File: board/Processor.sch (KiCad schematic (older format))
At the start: 12 parts, among them U1 TM4C123GH6PM

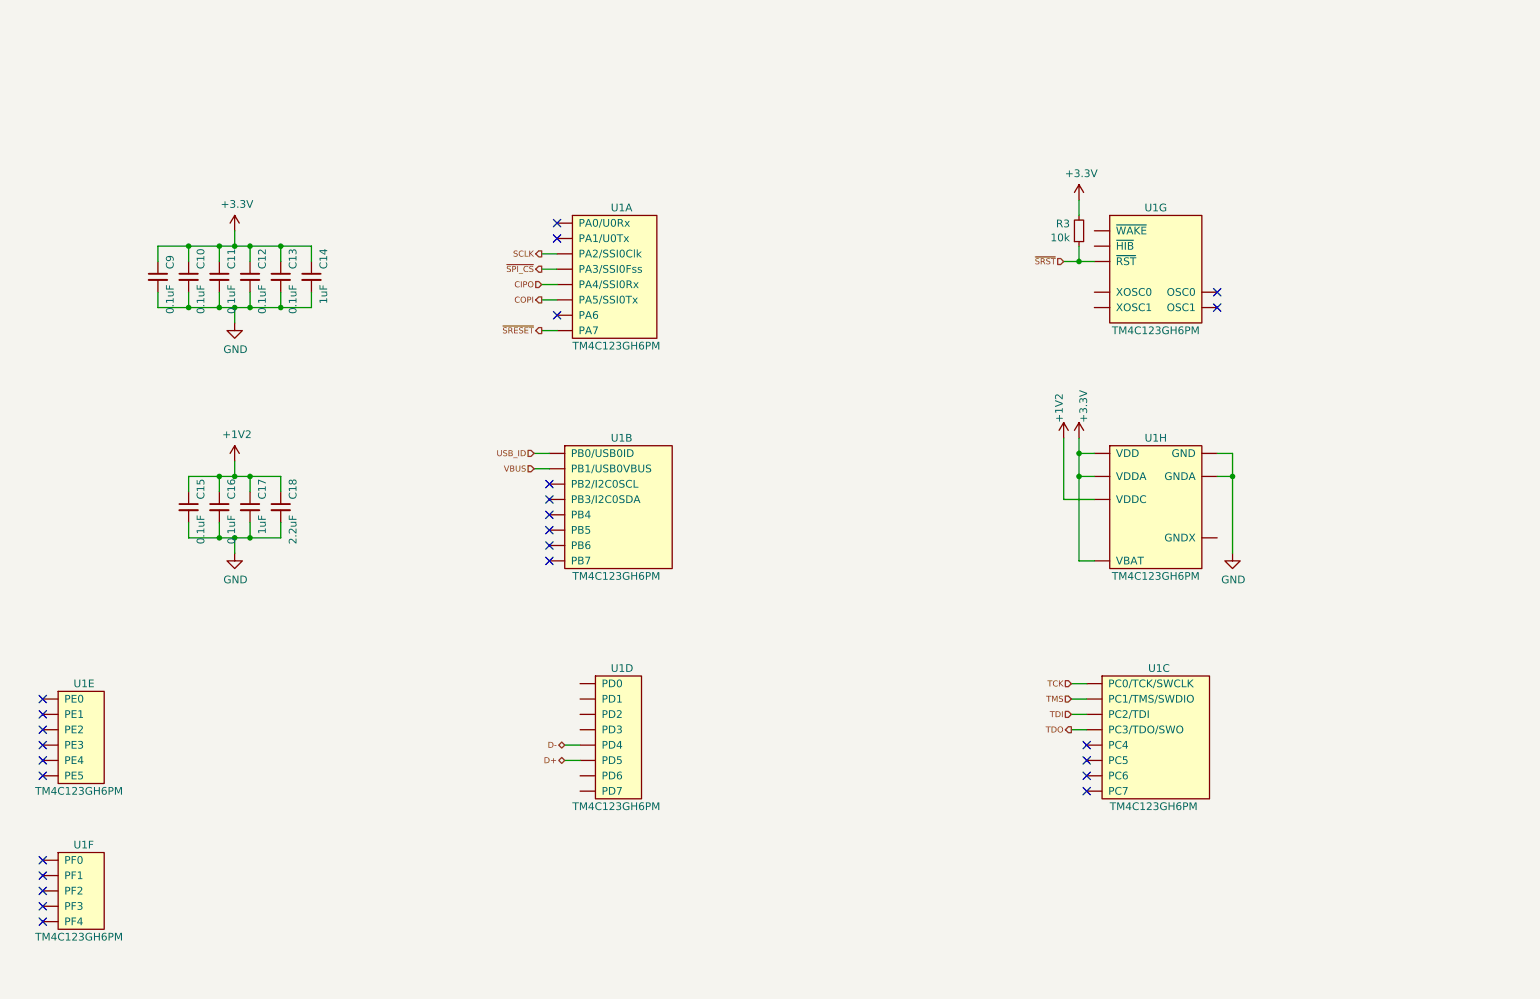
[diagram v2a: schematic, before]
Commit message: Added the two Flash devices and the user buttons to the schematic
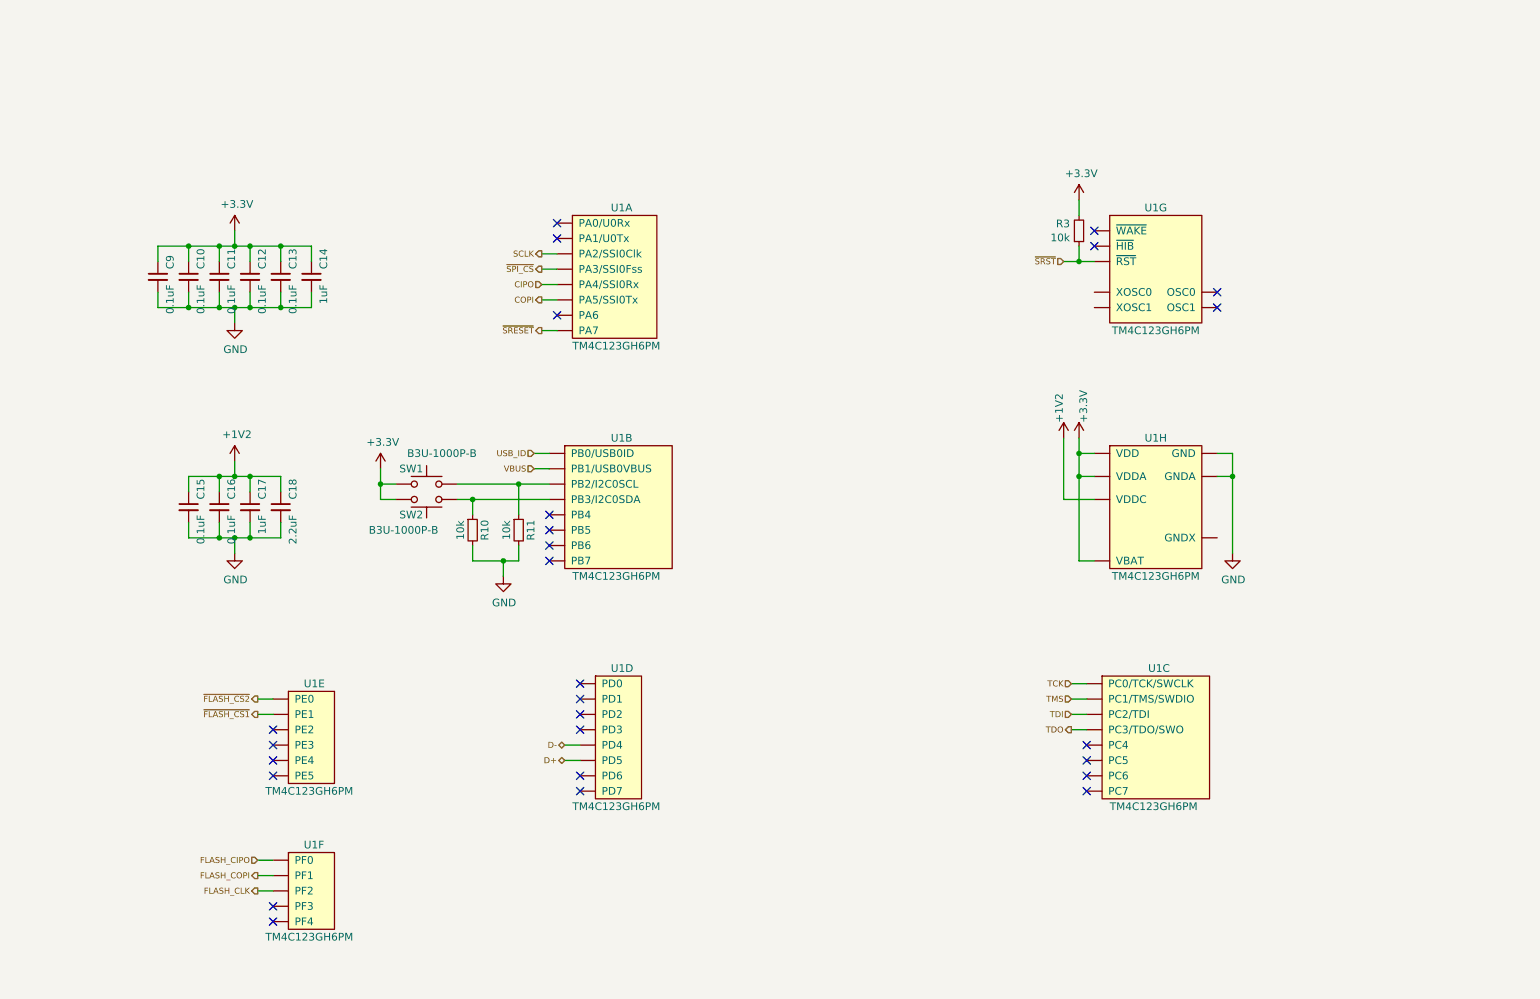
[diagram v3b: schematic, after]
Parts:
- added R10, R11: 10k, rhais_rcl:R0603, symbol Device:R_Small
- added SW1, SW2: B3U-1000P-B, rhais_button-smd:B3U-1000P-B, symbol Switch:SW_Push
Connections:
- net +3V3: now also SW1.1, SW2.1
- net GND: now also R10.2, R11.2
- net at U1.47 (PB2/I2C0SCL): now also R11.1, SW1.2
- net at U1.48 (PB3/I2C0SDA): now also R10.1, SW2.2
- net ~FLASH_CS1: now reaches U1.8 (PE1)
- net ~FLASH_CS2: now reaches U1.9 (PE0)
- net FLASH_CIPO: now reaches U1.28 (PF0)
- net FLASH_COPI: now reaches U1.29 (PF1)
- net FLASH_CLK: now reaches U1.30 (PF2)
- no-connect marks 26 -> 27
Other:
- moved on the sheet: U1E, U1F
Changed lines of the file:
@@
 $Descr A4 11693 8268
 encoding utf-8
-Sheet 3 4
+Sheet 3 5
 Title "Processor"
 Date ""
@@
 L DX_MON:TM4C123GH6PM U1
 U 5 1 5F0B1A2B
-P 1500 5500
-F 0 "U1" H 1450 5850 50  0000 L CNN
-F 1 "TM4C123GH6PM" H 1200 5150 50  0000 L CNN
-F 2 "DX-MON:QFP-64_10.2x10.2_Pitch0.5mm" H 1450 5500 50  0001 C CNN
-F 3 "" H 1450 5500 50  0001 C CNN
-F 4 "3008366" H 1500 4850 50  0001 C CNN "OC_FARNELL"
-F 5 "https://uk.farnell.com/texas-instruments/tm4c123gh6pmi/mcu-32bit-cortex-m4f-80mhz-lqfp/dp/3008366" H 1500 4950 50  0001 C CNN "URL_FARNELL"
-F 6 "Texas Instruments" H 1500 6050 50  0001 C CNN "MFR"
-F 7 "TM4C123GH6PM" H 1500 5950 50  0001 C CNN "MPN"
-	5    1500 5500
+P 3000 5500
+F 0 "U1" H 2950 5850 50  0000 L CNN
+F 1 "TM4C123GH6PM" H 2700 5150 50  0000 L CNN
+F 2 "DX-MON:QFP-64_10.2x10.2_Pitch0.5mm" H 2950 5500 50  0001 C CNN
+F 3 "" H 2950 5500 50  0001 C CNN
+F 4 "3008366" H 3000 4850 50  0001 C CNN "OC_FARNELL"
+F 5 "https://uk.farnell.com/texas-instruments/tm4c123gh6pmi/mcu-32bit-cortex-m4f-80mhz-lqfp/dp/3008366" H 3000 4950 50  0001 C CNN "URL_FARNELL"
+F 6 "Texas Instruments" H 3000 6050 50  0001 C CNN "MFR"
+F 7 "TM4C123GH6PM" H 3000 5950 50  0001 C CNN "MPN"
+	5    3000 5500
 	1    0    0    -1
 $EndComp
@@
 L DX_MON:TM4C123GH6PM U1
 U 6 1 5F0B3820
-P 1500 6500
-F 0 "U1" H 1450 6800 50  0000 L CNN
-F 1 "TM4C123GH6PM" H 1200 6200 50  0000 L CNN
-F 2 "DX-MON:QFP-64_10.2x10.2_Pitch0.5mm" H 1450 6500 50  0001 C CNN
-F 3 "" H 1450 6500 50  0001 C CNN
-F 4 "3008366" H 1500 5850 50  0001 C CNN "OC_FARNELL"
-F 5 "https://uk.farnell.com/texas-instruments/tm4c123gh6pmi/mcu-32bit-cortex-m4f-80mhz-lqfp/dp/3008366" H 1500 5950 50  0001 C CNN "URL_FARNELL"
-F 6 "Texas Instruments" H 1500 7050 50  0001 C CNN "MFR"
-F 7 "TM4C123GH6PM" H 1500 6950 50  0001 C CNN "MPN"
-	6    1500 6500
+P 3000 6500
+F 0 "U1" H 2950 6800 50  0000 L CNN
+F 1 "TM4C123GH6PM" H 2700 6200 50  0000 L CNN
+F 2 "DX-MON:QFP-64_10.2x10.2_Pitch0.5mm" H 2950 6500 50  0001 C CNN
+F 3 "" H 2950 6500 50  0001 C CNN
+F 4 "3008366" H 3000 5850 50  0001 C CNN "OC_FARNELL"
+F 5 "https://uk.farnell.com/texas-instruments/tm4c123gh6pmi/mcu-32bit-cortex-m4f-80mhz-lqfp/dp/3008366" H 3000 5950 50  0001 C CNN "URL_FARNELL"
+F 6 "Texas Instruments" H 3000 7050 50  0001 C CNN "MFR"
+F 7 "TM4C123GH6PM" H 3000 6950 50  0001 C CNN "MPN"
+	6    3000 6500
 	1    0    0    -1
 $EndComp
@@
 Wire Wire Line
 	2500 2300 2500 2200
-NoConn ~ 1250 5250
-NoConn ~ 1250 5350
-NoConn ~ 1250 5450
-NoConn ~ 1250 5550
-NoConn ~ 1250 5650
-NoConn ~ 1250 5750
-NoConn ~ 1250 6300
-NoConn ~ 1250 6400
-NoConn ~ 1250 6500
-NoConn ~ 1250 6600
-NoConn ~ 1250 6700
+NoConn ~ 4750 5850
+NoConn ~ 2750 6600
+NoConn ~ 2750 5450
+NoConn ~ 2750 5550
+NoConn ~ 2750 5650
+NoConn ~ 2750 5750
 NoConn ~ 8050 5550
 NoConn ~ 8050 5650
 NoConn ~ 8050 5750
 NoConn ~ 8050 5850
-NoConn ~ 4550 3850
-NoConn ~ 4550 3950
 NoConn ~ 4550 4050
 NoConn ~ 4550 4150
@@
 	1    0    0    -1
 $EndComp
+NoConn ~ 4750 5150
+NoConn ~ 4750 5250
+NoConn ~ 4750 5350
+NoConn ~ 4750 5450
+NoConn ~ 4750 5750
+NoConn ~ 8100 2200
+NoConn ~ 8100 2300
+Text HLabel 2650 6300 0    39   Input ~ 0
+FLASH_CIPO
+Text HLabel 2650 6400 0    39   Output ~ 0
+FLASH_COPI
+Text HLabel 2650 6500 0    39   Output ~ 0
+FLASH_CLK
+Text HLabel 2650 5350 0    39   Output ~ 0
+~FLASH_CS1
+NoConn ~ 2750 6700
+Wire Wire Line
+	2650 5350 2750 5350
+Wire Wire Line
+	2750 6500 2650 6500
+Wire Wire Line
+	2650 6400 2750 6400
+Wire Wire Line
+	2750 6300 2650 6300
+Text HLabel 2650 5250 0    39   Output ~ 0
+~FLASH_CS2
+Wire Wire Line
+	2650 5250 2750 5250
+$Comp
+L Switch:SW_Push SW1
+U 1 1 5F934F99
+P 3750 3850
+F 0 "SW1" H 3650 3950 50  0000 C CNN
+F 1 "B3U-1000P-B" H 3850 4050 50  0000 C CNN
+F 2 "rhais_button-smd:B3U-1000P-B" H 3750 4050 50  0001 C CNN
+F 3 "~" H 3750 4050 50  0001 C CNN
+	1    3750 3850
+	1    0    0    -1
+$EndComp
+$Comp
+L Switch:SW_Push SW2
+U 1 1 5F93C8F3
+P 3750 3950
+F 0 "SW2" H 3650 4050 50  0000 C CNN
+F 1 "B3U-1000P-B" H 3600 4150 50  0000 C CNN
+F 2 "rhais_button-smd:B3U-1000P-B" H 3750 4150 50  0001 C CNN
+F 3 "~" H 3750 4150 50  0001 C CNN
+	1    3750 3950
+	1    0    0    1
+$EndComp
+Wire Wire Line
+	3950 3950 4050 3950
+Wire Wire Line
+	3950 3850 4350 3850
+$Comp
+L Device:R_Small R10
+U 1 1 5F94EAA7
+P 4050 4150
+F 0 "R10" V 4100 4150 50  0000 C TNN
+F 1 "10k" V 4000 4150 50  0000 C BNN
+F 2 "rhais_rcl:R0603" H 4050 4150 50  0001 C CNN
+F 3 "~" H 4050 4150 50  0001 C CNN
+	1    4050 4150
+	1    0    0    -1
+$EndComp
+$Comp
+L Device:R_Small R11
+U 1 1 5F94F5F1
+P 4350 4150
+F 0 "R11" V 4400 4150 50  0000 C TNN
+F 1 "10k" V 4300 4150 50  0000 C BNN
+F 2 "rhais_rcl:R0603" H 4350 4150 50  0001 C CNN
+F 3 "~" H 4350 4150 50  0001 C CNN
+	1    4350 4150
+	1    0    0    -1
+$EndComp
+Wire Wire Line
+	4050 3950 4050 4050
+Connection ~ 4050 3950
+Wire Wire Line
+	4050 3950 4550 3950
+Wire Wire Line
+	4350 3850 4350 4050
+Connection ~ 4350 3850
+Wire Wire Line
+	4350 3850 4550 3850
+$Comp
+L power:GND #PWR036
+U 1 1 5F954FA2
+P 4250 4450
+F 0 "#PWR036" H 4250 4200 50  0001 C CNN
+F 1 "GND" H 4255 4277 50  0000 C CNN
+F 2 "" H 4250 4450 50  0001 C CNN
+F 3 "" H 4250 4450 50  0001 C CNN
+	1    4250 4450
+	1    0    0    -1
+$EndComp
+Wire Wire Line
+	4050 4250 4050 4350
+Wire Wire Line
+	4050 4350 4250 4350
+Wire Wire Line
+	4250 4350 4250 4450
+Wire Wire Line
+	4250 4350 4350 4350
+Wire Wire Line
+	4350 4350 4350 4250
+Connection ~ 4250 4350
+$Comp
+L power:+3.3V #PWR035
+U 1 1 5F979C91
+P 3450 3750
+F 0 "#PWR035" H 3450 3600 50  0001 C CNN
+F 1 "+3.3V" H 3465 3923 50  0000 C CNN
+F 2 "" H 3450 3750 50  0001 C CNN
+F 3 "" H 3450 3750 50  0001 C CNN
+	1    3450 3750
+	1    0    0    -1
+$EndComp
+Wire Wire Line
+	3450 3750 3450 3850
+Wire Wire Line
+	3450 3850 3550 3850
+Wire Wire Line
+	3550 3950 3450 3950
+Wire Wire Line
+	3450 3950 3450 3850
+Connection ~ 3450 3850
 $EndSCHEMATC

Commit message: Added a status LED for the phase of flash programming in progress, and a crystal so the USB peripheral can be used
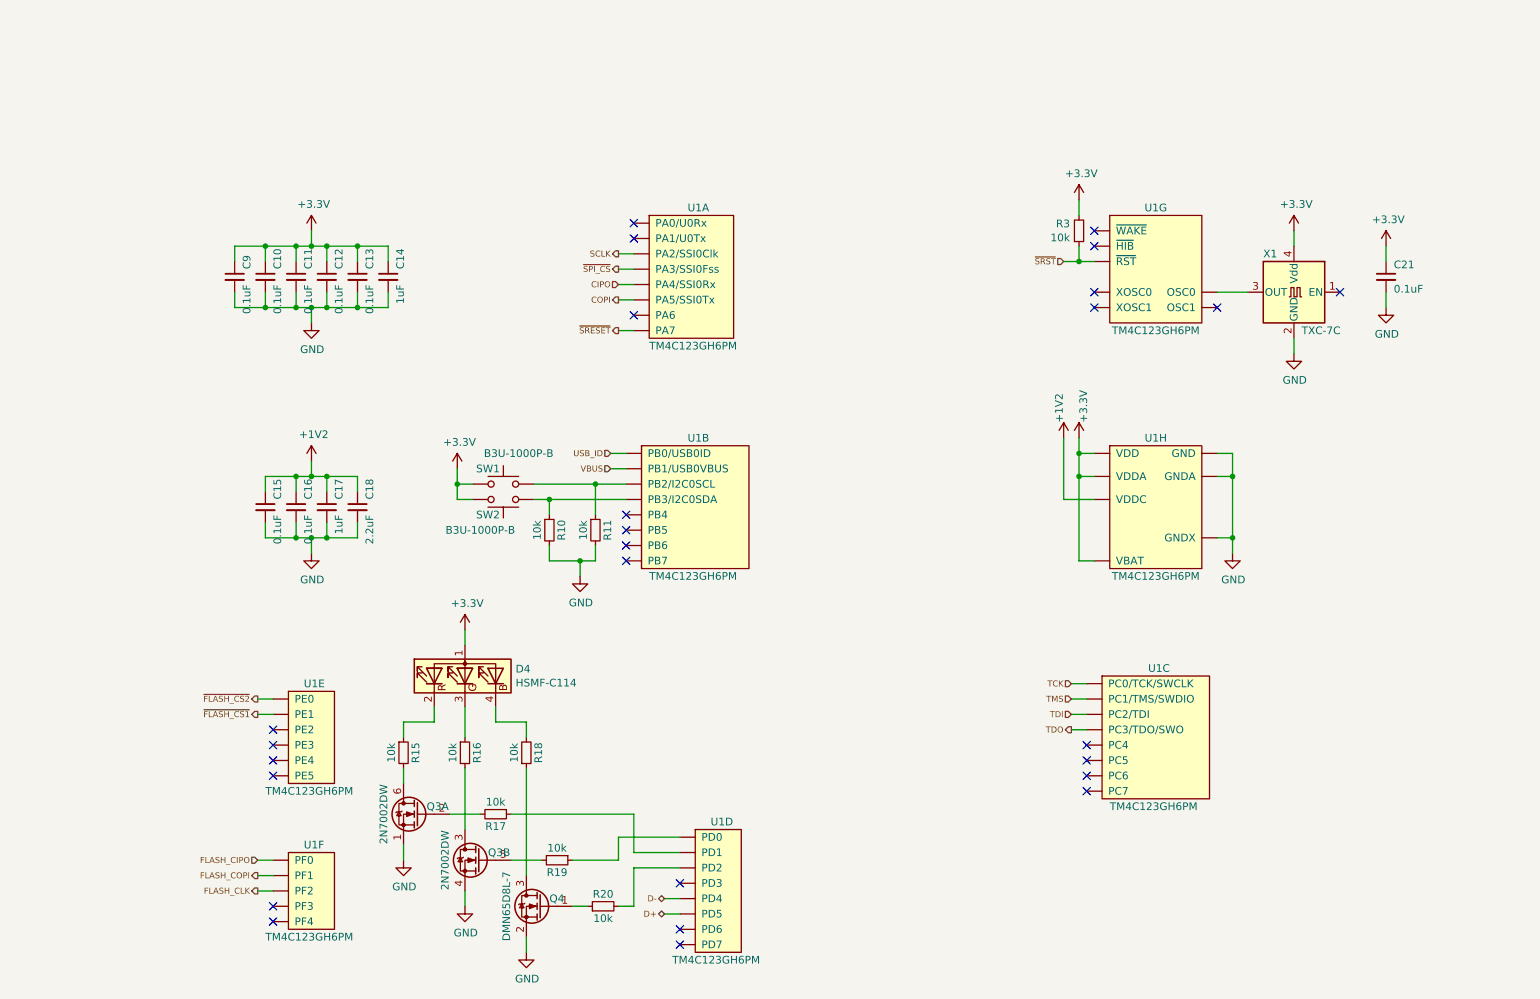
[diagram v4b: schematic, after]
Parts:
- added C21: 0.1uF, rhais_rcl:C0603, symbol Device:C_Small
- added D4: HSMF-C114, rhais_led:LED0606, symbol Device:LED_ARGB
- added Q3: 2N7002DW, rhais_package-smd:SOT-363_SC-70-6, symbol Device:Q_DUAL_NMOS_S1G1D2S2G2D1
- added Q4: DMN65D8L-7, rhais_package-smd:SOT-23, symbol Device:Q_NMOS_GSD
- added R15, R16, R17, R18, R19, R20: 10k, rhais_rcl:R0603, symbol Device:R_Small
- added X1: TXC-7C, rhais_osc:SMD3225, symbol Oscillator:TXC-7C
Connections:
- net +3V3: now also C21.1, D4.1 (A), X1.4 (Vdd)
- net GND: now also U1.35 (GNDX), C21.2, Q3.1 (S), Q3.4 (S), Q4.2 (S), X1.2 (GND)
- net at U1.61 (PD0): now also R19.1
- net at U1.62 (PD1): now also R17.1
- net at U1.63 (PD2): now also R20.2
- net at U1.40 (OSC0): now also X1.3 (OUT)
- new net: D4.2 (RK), R15.1
- new net: D4.3 (GK), R16.1
- new net: D4.4 (BK), R18.2
- new net: Q4.1 (G), R20.1
- new net: Q4.3 (D), R18.1
- new net: Q3.2 (G), R17.2
- new net: Q3.6 (D), R15.2
- new net: Q3.3 (D), R16.2
- new net: Q3.5 (G), R19.2
- no-connect marks 27 -> 26
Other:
- moved on the sheet: C10, C11, C12, C13, C14, C15, C16, C17, C18, C9, R10, R11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

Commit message: Fixed the state of the BOM for the PCB being horrid
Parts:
- C10, C11, C12, C13, C15, C16, C21, C9: MFR (none) -> Multicomp; MPN (none) -> MC0603B104J250CT; OC_FARNELL (none) -> 2310559; URL_FARNELL (none) -> https://uk.farnell.com/multicomp/mc0603b104j250ct/cap-0-1-f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
- C14, C17: MFR (none) -> Multicomp; MPN (none) -> MC0603B105K160CT; OC_FARNELL (none) -> 2320814; URL_FARNELL (none) -> https://uk.farnell.com/multicomp/mc0603b105k160ct/cap-1-f-1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
- C18: MFR (none) -> TDK; MPN (none) -> C1608X5R1C225K080AB; OC_FARNELL (none) -> 2211169; URL_FARNELL (none) -> https://uk.farnell.com/tdk/c1608x5r1c225k080ab/cap-2-2-f-16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
- Q4: MFR (none) -> Diodes Inc; MPN (none) -> DMN65D8L-7; OC_FARNELL (none) -> 2543546; URL_FARNELL (none) -> https://uk.farnell.com/diodes-inc/dmn65d8l-7/mosfet-n-ch-20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
- R10, R11, R15, R16, R17, R18, R19, R20, R3: MFR (none) -> Multicomp; MPN (none) -> MC0063W0603110K; OC_FARNELL (none) -> 2130939; URL_FARNELL (none) -> https://uk.farnell.com/multicomp/mc0063w0603110k/res-10k-1-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
- SW1, SW2: MFR (none) -> Omron; MPN (none) -> B3U-1000P-B; OC_FARNELL (none) -> 1333654; URL_FARNELL (none) -> https://uk.farnell.com/omron/b3u-1000p-b/switch-spst-no-0-0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
- X1: MFR (none) -> Multicomp; MPN (none) -> MCSJK-3N-25.00-3.3-50-B; OC_FARNELL (none) -> 2854308; URL_FARNELL (none) -> https://uk.farnell.com/multicomp/mcsjk-3n-25-00-3-3-50-b/os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

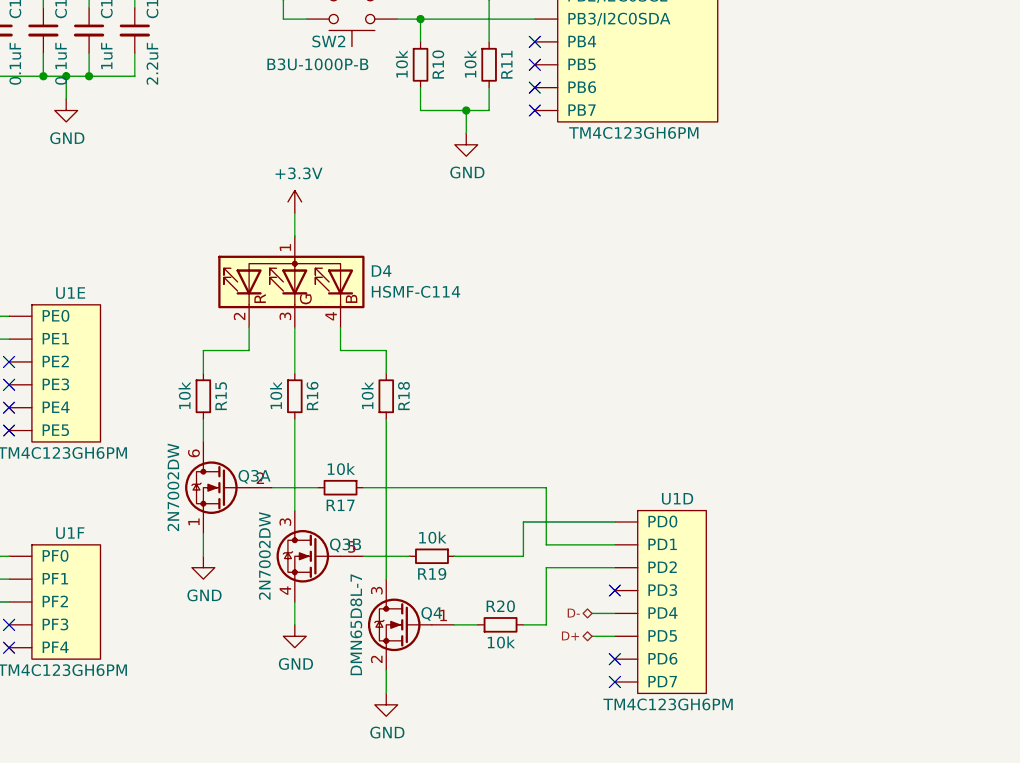
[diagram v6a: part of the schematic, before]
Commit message: Fixed the layout of the RGB LED support components and the values of the resistors for setting the current through the LEDs
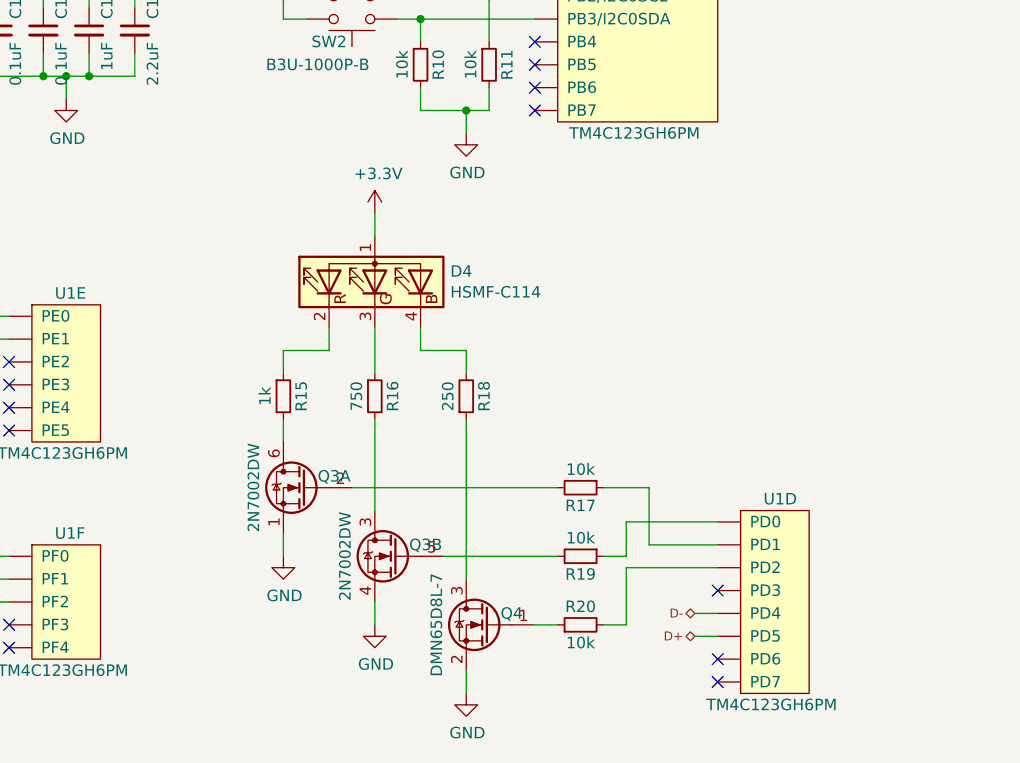
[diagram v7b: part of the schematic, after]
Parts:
- R15: value 10k -> 1k
- R16: value 10k -> 750
- R18: value 10k -> 250
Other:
- moved on the sheet: D4, Q3A, Q3B, Q4, R15, R16, R17, R18, R19, R20, U1D
